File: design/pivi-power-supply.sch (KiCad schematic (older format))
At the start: 3 parts, among them U7 TLV70233DBV

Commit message: Fix #4: add GPIO to reset microcontroller from pi.
* Add a Raspeberry pi pin (GPIO 18) to reset microcontroller.
* Add a Raspebeery pi pin (GPIO 23) to control the microcontroller status.
* Add a RGB LED connected to the microcontroller (PD0, PD1, PD2).
* Rename all the sheets to PIVI v1.1.
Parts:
- C52, C53: symbol C -> C-RESCUE-pivi-shield
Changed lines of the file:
@@
 EESchema Schematic File Version 2
+LIBS:pivi-shield-rescue
 LIBS:power
 LIBS:device
@@
 LIBS:memory
 LIBS:xilinx
-LIBS:special
 LIBS:microcontrollers
 LIBS:dsp
@@
 LIBS:txs0104e
 LIBS:less
+LIBS:pivi-shield-cache
 EELAYER 25 0
 EELAYER END
@@
 Sheet 8 12
 Title "PIVI"
-Date "sáb 01 nov 2014"
-Rev "1.0"
+Date "mar 23 jun 2015"
+Rev "1.1"
 Comp "Copyright (C) LESS industries S.A. 2014,2015"
 Comment1 "Share alike attribution non-commercial 4.0"
@@
 $EndComp
 $Comp
-L C C53
+L C-RESCUE-pivi-shield C53
 U 1 1 548CB8AD
 P 7150 3525
+AR Path="/548CB8AD" Ref="C53"  Part="1"
+AR Path="/548F00C8/548CB8AD" Ref="C53"  Part="1"
 F 0 "C53" H 7175 3600 40  0000 L CNN
 F 1 "1uF" H 7175 3425 40  0000 L CNN
@@
 	7150 3175 7150 3325
 $Comp
-L +5V #PWR057
+L +5V #PWR058
 U 1 1 548CBAAB
 P 5650 3175
-F 0 "#PWR057" H 5650 3265 20  0001 C CNN
+F 0 "#PWR058" H 5650 3265 20  0001 C CNN
 F 1 "+5V" H 5650 3300 30  0000 C CNN
 F 2 "" H 5650 3175 60  0000 C CNN
@@
 $EndComp
 $Comp
-L C C52
+L C-RESCUE-pivi-shield C52
 U 1 1 548CB868
 P 5650 3500
+AR Path="/548CB868" Ref="C52"  Part="1"
+AR Path="/548F00C8/548CB868" Ref="C52"  Part="1"
 F 0 "C52" H 5675 3575 40  0000 L CNN
 F 1 "100nF" H 5675 3400 40  0000 L CNN
@@
 	7150 3775 7150 3725
 $Comp
-L +3V3 #PWR058
+L +3V3 #PWR059
 U 1 1 54965F4C
 P 7150 3175
-F 0 "#PWR058" H 7150 3025 60  0001 C CNN
+F 0 "#PWR059" H 7150 3025 60  0001 C CNN
 F 1 "+3V3" H 7150 3300 30  0000 C CNN
 F 2 "" H 7150 3175 60  0000 C CNN
@@
 $EndComp
 $Comp
-L GND #PWR059
+L GND-RESCUE-pivi-shield #PWR060
 U 1 1 54BFA945
 P 5650 3750
-F 0 "#PWR059" H 5650 3500 60  0001 C CNN
+F 0 "#PWR060" H 5650 3500 60  0001 C CNN
 F 1 "GND" H 5650 3600 60  0000 C CNN
 F 2 "" H 5650 3750 60  0000 C CNN
@@
 $EndComp
 $Comp
-L GND #PWR060
+L GND-RESCUE-pivi-shield #PWR061
 U 1 1 54BFA959
 P 6400 3750
-F 0 "#PWR060" H 6400 3500 60  0001 C CNN
+F 0 "#PWR061" H 6400 3500 60  0001 C CNN
 F 1 "GND" H 6400 3600 60  0000 C CNN
 F 2 "" H 6400 3750 60  0000 C CNN
@@
 $EndComp
 $Comp
-L GND #PWR061
+L GND-RESCUE-pivi-shield #PWR062
 U 1 1 54BFA96D
 P 7150 3775
-F 0 "#PWR061" H 7150 3525 60  0001 C CNN
+F 0 "#PWR062" H 7150 3525 60  0001 C CNN
 F 1 "GND" H 7150 3625 60  0000 C CNN
 F 2 "" H 7150 3775 60  0000 C CNN

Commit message: Fix #4: Move RGB LED from microcontroller to pi.
* Move RGB LED. Now it is controlled by the raspberry pi.
* Change some new libraries for capacitors and resistors.
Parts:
- C52, C53: symbol C-RESCUE-pivi-shield -> C
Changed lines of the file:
@@
 LIBS:txs0104e
 LIBS:less
-LIBS:pivi-shield-cache
 EELAYER 25 0
 EELAYER END
@@
 $EndComp
 $Comp
-L C-RESCUE-pivi-shield C53
+L C C53
 U 1 1 548CB8AD
 P 7150 3525
@@
 $EndComp
 Wire Wire Line
-	5650 3750 5650 3700
+	5650 3650 5650 3750
 Wire Wire Line
 	6850 3300 7150 3300
 Wire Wire Line
-	5650 3300 5650 3175
+	5650 3175 5650 3350
 Wire Wire Line
-	7150 3175 7150 3325
+	7150 3175 7150 3375
 $Comp
 L +5V #PWR058
@@
 $EndComp
 $Comp
-L C-RESCUE-pivi-shield C52
+L C C52
 U 1 1 548CB868
 P 5650 3500
@@
 	6400 3750 6400 3650
 Wire Wire Line
-	7150 3775 7150 3725
+	7150 3675 7150 3775
 $Comp
 L +3V3 #PWR059
@@
 $EndComp
 Connection ~ 7150 3300
+Connection ~ 5650 3300
 $EndSCHEMATC

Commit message: Changing footprints of  audio jack3.5mm Added new footprints. Added debub uart,  reference voltage Added two extra circuits for voltage measure Moving to PIVI 2.0, added circuits for current clamps
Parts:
- renumbered C52 to C12, C53 to C13, U7 to U3
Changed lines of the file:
@@
 EESchema Schematic File Version 2
-LIBS:pivi-shield-rescue
 LIBS:power
 LIBS:device
@@
 LIBS:txs0104e
 LIBS:less
+LIBS:pivi-shield-cache
 EELAYER 25 0
 EELAYER END
 $Descr A4 11693 8268
 encoding utf-8
-Sheet 8 12
+Sheet 10 20
 Title "PIVI"
-Date "mar 23 jun 2015"
-Rev "1.1"
+Date "Mon 27 Jul 2015"
+Rev "2.0"
 Comp "Copyright (C) LESS industries S.A. 2014,2015"
 Comment1 "Share alike attribution non-commercial 4.0"
@@
 $EndDescr
 $Comp
-L TLV70233DBV U7
+L TLV70233DBV U3
 U 1 1 548CB80E
 P 6400 3350
-F 0 "U7" H 6150 3550 40  0000 C CNN
+F 0 "U3" H 6150 3550 40  0000 C CNN
 F 1 "TLV70233DBV" H 6500 3550 40  0000 C CNN
 F 2 "SMD_Packages:SOT-23-5" H 6400 3625 35  0000 C CIN
@@
 $EndComp
 $Comp
-L C C53
+L C C13
 U 1 1 548CB8AD
 P 7150 3525
-AR Path="/548CB8AD" Ref="C53"  Part="1"
-AR Path="/548F00C8/548CB8AD" Ref="C53"  Part="1"
-F 0 "C53" H 7175 3600 40  0000 L CNN
+F 0 "C13" H 7175 3600 40  0000 L CNN
 F 1 "1uF" H 7175 3425 40  0000 L CNN
 F 2 "Capacitors_SMD:C_0603" H 7450 3375 30  0000 C CNN
@@
 	7150 3175 7150 3375
 $Comp
-L +5V #PWR058
+L +5V #PWR44
 U 1 1 548CBAAB
 P 5650 3175
-F 0 "#PWR058" H 5650 3265 20  0001 C CNN
+F 0 "#PWR44" H 5650 3265 20  0001 C CNN
 F 1 "+5V" H 5650 3300 30  0000 C CNN
 F 2 "" H 5650 3175 60  0000 C CNN
@@
 $EndComp
 $Comp
-L C C52
+L C C12
 U 1 1 548CB868
 P 5650 3500
-AR Path="/548CB868" Ref="C52"  Part="1"
-AR Path="/548F00C8/548CB868" Ref="C52"  Part="1"
-F 0 "C52" H 5675 3575 40  0000 L CNN
+F 0 "C12" H 5675 3575 40  0000 L CNN
 F 1 "100nF" H 5675 3400 40  0000 L CNN
 F 2 "Capacitors_SMD:C_0603" H 5950 3325 30  0000 C CNN
@@
 	7150 3675 7150 3775
 $Comp
-L +3V3 #PWR059
+L +3V3 #PWR47
 U 1 1 54965F4C
 P 7150 3175
-F 0 "#PWR059" H 7150 3025 60  0001 C CNN
+F 0 "#PWR47" H 7150 3025 60  0001 C CNN
 F 1 "+3V3" H 7150 3300 30  0000 C CNN
 F 2 "" H 7150 3175 60  0000 C CNN
@@
 $EndComp
 $Comp
-L GND-RESCUE-pivi-shield #PWR060
+L GND #PWR45
 U 1 1 54BFA945
 P 5650 3750
-F 0 "#PWR060" H 5650 3500 60  0001 C CNN
+F 0 "#PWR45" H 5650 3500 60  0001 C CNN
 F 1 "GND" H 5650 3600 60  0000 C CNN
 F 2 "" H 5650 3750 60  0000 C CNN
@@
 $EndComp
 $Comp
-L GND-RESCUE-pivi-shield #PWR061
+L GND #PWR46
 U 1 1 54BFA959
 P 6400 3750
-F 0 "#PWR061" H 6400 3500 60  0001 C CNN
+F 0 "#PWR46" H 6400 3500 60  0001 C CNN
 F 1 "GND" H 6400 3600 60  0000 C CNN
 F 2 "" H 6400 3750 60  0000 C CNN
@@
 $EndComp
 $Comp
-L GND-RESCUE-pivi-shield #PWR062
+L GND #PWR48
 U 1 1 54BFA96D
 P 7150 3775
-F 0 "#PWR062" H 7150 3525 60  0001 C CNN
+F 0 "#PWR48" H 7150 3525 60  0001 C CNN
 F 1 "GND" H 7150 3625 60  0000 C CNN
 F 2 "" H 7150 3775 60  0000 C CNN

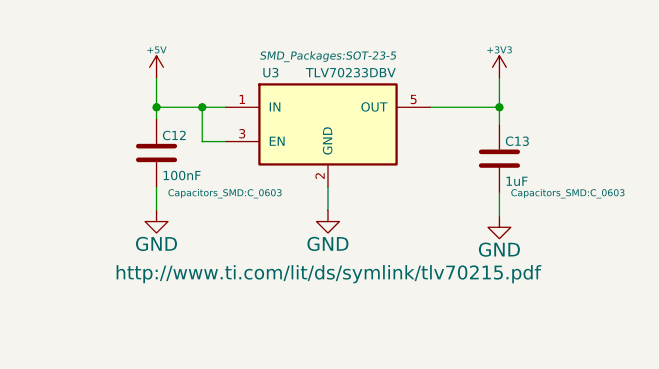
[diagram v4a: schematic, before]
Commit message: PCB routed + BOM complete
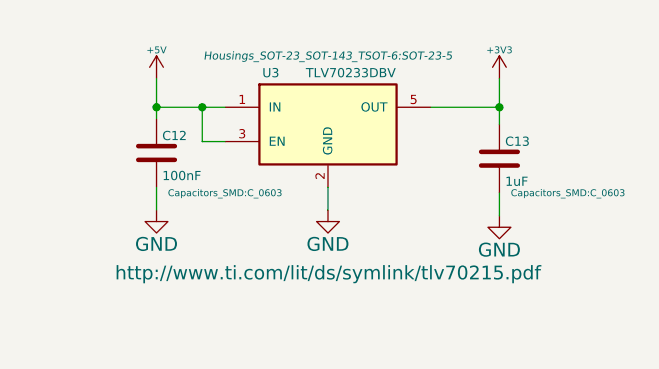
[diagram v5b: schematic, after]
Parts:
- U3: footprint SMD_Packages:SOT-23-5 -> Housings_SOT-23_SOT-143_TSOT-6:SOT-23-5
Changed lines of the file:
@@
 F 0 "U3" H 6150 3550 40  0000 C CNN
 F 1 "TLV70233DBV" H 6500 3550 40  0000 C CNN
-F 2 "SMD_Packages:SOT-23-5" H 6400 3625 35  0000 C CIN
+F 2 "Housings_SOT-23_SOT-143_TSOT-6:SOT-23-5" H 6400 3625 35  0000 C CIN
 F 3 "http://www.ti.com/lit/ds/symlink/tlv70215.pdf" H 6400 2675 60  0000 C CNN
 	1    6400 3350
